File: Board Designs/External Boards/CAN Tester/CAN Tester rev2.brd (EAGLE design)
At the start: 83.8 x 100.3 mm, 27 parts, among them M1 Minifit, M2 Nanofit, M3 Nanofit-1, M4 Minifit-1, U1 ISOLATED CAN TRANSCIEVER, U3 TEENSY_3.2_SIMPLE, U4 CHARACTER_LCD

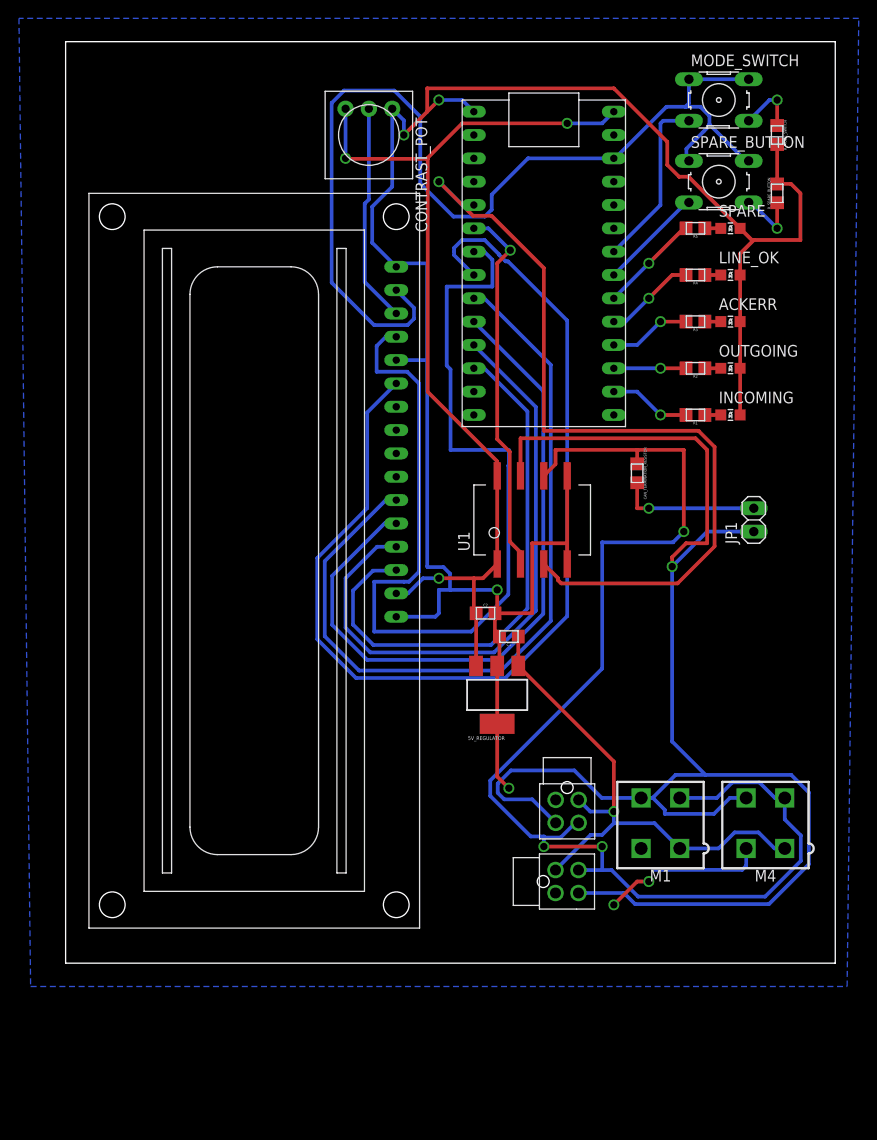
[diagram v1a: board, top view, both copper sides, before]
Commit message: Updated with true isolation for separate 5V for the isocan and teensy
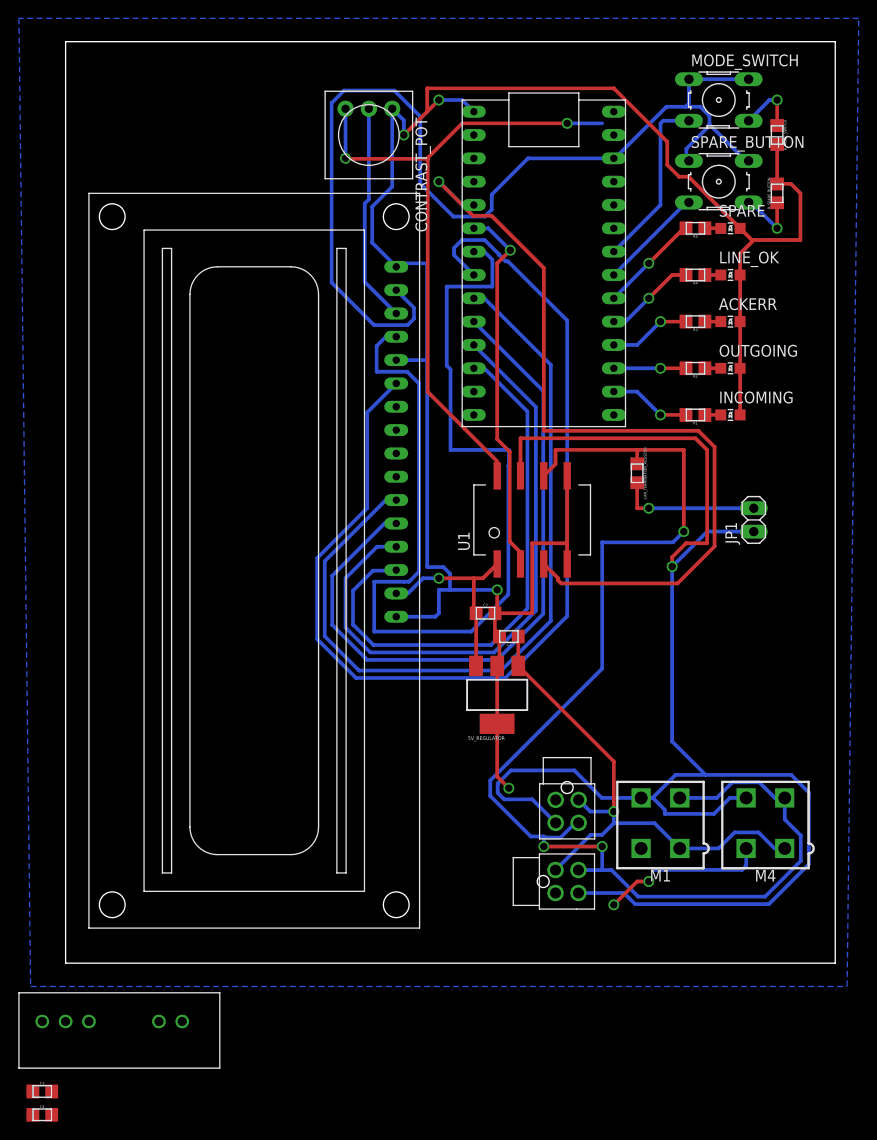
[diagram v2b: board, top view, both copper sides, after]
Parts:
- added C3, C4: 10 uF, HyTechDevices:0805
- added U$1: NCS1S1205SC-12V-5VCONVERTER, HyTechDevices:DCDC-CONVERTER
- R_MODE_SWITCH, R_SPARE_BUTTON: value 27K -> 10K
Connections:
- new net +5V_ISOLATED: C3.1, CONTRAST_POT.3, U$1.+VOUT, U1.P$1, U3.VIN, U4.15
- new net GND_ISOLATED: C3.2, U$1.-VOUT
- net +12V: now also C4.1, U$1.+VIN
- net +5V: no longer CONTRAST_POT.3, U1.P$1, U3.VIN, U4.15
- net GND: now also C4.2, U$1.-VIN
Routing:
- net +5V: track 106.1 -> 5.74 mm, vias 3 -> 0
- net +5V_ISOLATED: track 0.00 -> 87.0 mm, vias 0 -> 3
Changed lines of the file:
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@@
 <attribute name="VALUE" x="68.58" y="79.4512" size="0.3048" layer="27" rot="R180" align="top-center"/>
 </element>
-<element name="R_MODE_SWITCH" library="HyTechDevices" package="0805" value="27K" x="77.47" y="88.9" smashed="yes" rot="R270">
+<element name="R_MODE_SWITCH" library="HyTechDevices" package="0805" value="10K" x="77.47" y="88.9" smashed="yes" rot="R270">
 <attribute name="NAME" x="78.1939" y="88.9" size="0.3048" layer="25" rot="R270" align="bottom-center"/>
 <attribute name="VALUE" x="76.7588" y="88.9" size="0.3048" layer="27" rot="R270" align="top-center"/>
 </element>
-<element name="R_SPARE_BUTTON" library="HyTechDevices" package="0805" value="27K" x="77.47" y="82.55" smashed="yes" rot="R90">
+<element name="R_SPARE_BUTTON" library="HyTechDevices" package="0805" value="10K" x="77.47" y="82.55" smashed="yes" rot="R90">
 <attribute name="NAME" x="76.7461" y="82.55" size="0.3048" layer="25" rot="R90" align="bottom-center"/>
 <attribute name="VALUE" x="78.1812" y="82.55" size="0.3048" layer="27" rot="R90" align="top-center"/>
@@
 <attribute name="NAME" x="73.1012" y="44.3738" size="1.27" layer="25" ratio="10" rot="R90"/>
 <attribute name="VALUE" x="78.105" y="44.45" size="1.27" layer="27" rot="R90"/>
+</element>
+<element name="U$1" library="HyTechDevices" package="DCDC-CONVERTER" value="NCS1S1205SC-12V-5VCONVERTER" x="6.35" y="-7.62" smashed="yes"/>
+<element name="C3" library="HyTechDevices" package="0805" value="10 uF" x="-2.54" y="-15.24" smashed="yes">
+<attribute name="NAME" x="-2.54" y="-14.5161" size="0.3048" layer="25" align="bottom-center"/>
+<attribute name="VALUE" x="-2.54" y="-15.9512" size="0.3048" layer="27" align="top-center"/>
+</element>
+<element name="C4" library="HyTechDevices" package="0805" value="10 uF" x="-2.54" y="-17.78" smashed="yes">
+<attribute name="NAME" x="-2.54" y="-17.0561" size="0.3048" layer="25" align="bottom-center"/>
+<attribute name="VALUE" x="-2.54" y="-18.4912" size="0.3048" layer="27" align="top-center"/>
 </element>
 </elements>
@@
 <wire x1="50.8" y1="36.83" x2="50.8" y2="44.45" width="0.4064" layer="1"/>
 <wire x1="50.8" y1="44.45" x2="54.61" y2="44.45" width="0.4064" layer="1"/>
+<contactref element="C4" pad="2"/>
+<contactref element="U$1" pad="-VIN"/>
+<wire x1="63.94" y1="8.89" x2="62.67" y2="11.22" width="0" layer="19" extent="16-16"/>
+<wire x1="63.5" y1="7.62" x2="63.94" y2="8.89" width="0" layer="19" extent="16-16"/>
+<wire x1="53.34" y1="6.37" x2="59.69" y2="5.08" width="0" layer="19" extent="1-1"/>
+<wire x1="53.36" y1="16.51" x2="53.34" y2="6.37" width="0" layer="19" extent="1-1"/>
+<wire x1="48.26" y1="17.78" x2="53.36" y2="16.51" width="0" layer="19" extent="1-1"/>
+<wire x1="-2.54" y1="-7.62" x2="46.99" y2="19.05" width="0" layer="19" extent="1-1"/>
+<wire x1="-1.515" y1="-17.78" x2="-2.54" y2="-7.62" width="0" layer="19" extent="1-1"/>
 </signal>
 <signal name="CANH">
@@
 <wire x1="70.0024" y1="89.9414" x2="70.104" y2="90.043" width="0.4064" layer="16"/>
 </signal>
-<signal name="+5V">
-<contactref element="U3" pad="VIN"/>
-<contactref element="5V_REGULATOR" pad="3"/>
-<contactref element="C2" pad="1"/>
-<contactref element="U1" pad="P$1"/>
-<contactref element="U1" pad="P$8"/>
-<contactref element="U4" pad="15"/>
-<contactref element="CONTRAST_POT" pad="3"/>
-<wire x1="46.99" y1="42.19" x2="46.99" y2="51.79" width="0.4064" layer="1"/>
-<wire x1="46.99" y1="42.19" x2="45.44" y2="40.64" width="0.4064" layer="1"/>
-<wire x1="45.44" y1="40.64" x2="44.45" y2="40.64" width="0.4064" layer="1"/>
-<wire x1="44.45" y1="40.64" x2="44.45" y2="37.075" width="0.4064" layer="1"/>
-<wire x1="44.45" y1="37.075" x2="44.695" y2="36.83" width="0.4064" layer="1"/>
-<wire x1="44.695" y1="36.83" x2="44.695" y2="31.095" width="0.4064" layer="1"/>
-<wire x1="44.695" y1="31.095" x2="44.69" y2="31.09" width="0.4064" layer="1"/>
-<wire x1="44.45" y1="40.64" x2="40.64" y2="40.64" width="0.4064" layer="1"/>
-<via x="40.64" y="40.64" extent="1-16" drill="0.8" diameter="0.8"/>
-<wire x1="40.64" y1="40.64" x2="38.92" y2="40.64" width="0.4064" layer="16"/>
-<wire x1="38.92" y1="40.64" x2="37.27" y2="38.99" width="0.4064" layer="16"/>
-<wire x1="37.27" y1="38.99" x2="36" y2="38.99" width="0.4064" layer="16"/>
-<wire x1="46.99" y1="51.79" x2="46.99" y2="53.36670625" width="0.4064" layer="1"/>
-<wire x1="39.4272" y1="86.3028" x2="39.37" y2="86.36" width="0.4064" layer="1"/>
-<wire x1="46.99" y1="53.36670625" x2="39.4272" y2="60.92950625" width="0.4064" layer="1"/>
-<wire x1="39.4272" y1="60.92950625" x2="39.4272" y2="86.3028" width="0.4064" layer="1"/>
-<wire x1="39.37" y1="86.36" x2="43.18" y2="90.17" width="0.4064" layer="1"/>
-<wire x1="43.18" y1="90.17" x2="54.61" y2="90.17" width="0.4064" layer="1"/>
-<via x="54.61" y="90.17" extent="1-16" drill="0.8" diameter="0.8"/>
-<wire x1="54.61" y1="90.17" x2="58.42" y2="90.17" width="0.4064" layer="16"/>
-<wire x1="58.42" y1="90.17" x2="59.69" y2="91.44" width="0.4064" layer="16"/>
-<wire x1="39.4272" y1="86.3028" x2="30.5372" y2="86.3028" width="0.4064" layer="1"/>
-<wire x1="30.5372" y1="86.3028" x2="30.48" y2="86.36" width="0.4064" layer="1"/>
-<via x="30.48" y="86.36" extent="1-16" drill="0.8" diameter="0.8"/>
-<wire x1="30.48" y1="86.36" x2="30.48" y2="91.7575" width="0.4064" layer="16"/>
-</signal>
 <signal name="N$13">
 <contactref element="U3" pad="A6"/>
@@
 <wire x1="58.42" y1="12.7" x2="59.69" y2="13.97" width="0.4064" layer="16"/>
 <wire x1="57.17" y1="12.7" x2="58.42" y2="12.7" width="0.4064" layer="16"/>
+<contactref element="C4" pad="1"/>
+<contactref element="U$1" pad="+VIN"/>
+<wire x1="0" y1="-7.62" x2="53.34" y2="8.87" width="0" layer="19" extent="1-1"/>
+<wire x1="-3.565" y1="-17.78" x2="0" y2="-7.62" width="0" layer="19" extent="1-1"/>
 </signal>
 <signal name="N$12">
@@
 <wire x1="63.5" y1="48.26" x2="74.93" y2="48.26" width="0.4064" layer="16"/>
 </signal>
+<signal name="+5V_ISOLATED">
+<contactref element="U$1" pad="+VOUT"/>
+<contactref element="C3" pad="1"/>
+<contactref element="U3" pad="VIN"/>
+<contactref element="U1" pad="P$1"/>
+<contactref element="U4" pad="15"/>
+<contactref element="CONTRAST_POT" pad="3"/>
+<wire x1="46.99" y1="42.19" x2="45.44" y2="40.64" width="0.4064" layer="1"/>
+<wire x1="45.44" y1="40.64" x2="44.45" y2="40.64" width="0.4064" layer="1"/>
+<wire x1="44.45" y1="40.64" x2="44.45" y2="37.075" width="0.4064" layer="1"/>
+<wire x1="44.45" y1="40.64" x2="40.64" y2="40.64" width="0.4064" layer="1"/>
+<via x="40.64" y="40.64" extent="1-16" drill="0.8" diameter="0.8"/>
+<wire x1="40.64" y1="40.64" x2="38.92" y2="40.64" width="0.4064" layer="16"/>
+<wire x1="38.92" y1="40.64" x2="37.27" y2="38.99" width="0.4064" layer="16"/>
+<wire x1="37.27" y1="38.99" x2="36" y2="38.99" width="0.4064" layer="16"/>
+<wire x1="39.4272" y1="86.3028" x2="39.37" y2="86.36" width="0.4064" layer="1"/>
+<wire x1="46.99" y1="53.36670625" x2="39.4272" y2="60.92950625" width="0.4064" layer="1"/>
+<wire x1="39.4272" y1="60.92950625" x2="39.4272" y2="86.3028" width="0.4064" layer="1"/>
+<wire x1="39.37" y1="86.36" x2="43.18" y2="90.17" width="0.4064" layer="1"/>
+<wire x1="43.18" y1="90.17" x2="54.61" y2="90.17" width="0.4064" layer="1"/>
+<via x="54.61" y="90.17" extent="1-16" drill="0.8" diameter="0.8"/>
+<wire x1="54.61" y1="90.17" x2="58.42" y2="90.17" width="0.4064" layer="16"/>
+<wire x1="39.4272" y1="86.3028" x2="30.5372" y2="86.3028" width="0.4064" layer="1"/>
+<wire x1="30.5372" y1="86.3028" x2="30.48" y2="86.36" width="0.4064" layer="1"/>
+<via x="30.48" y="86.36" extent="1-16" drill="0.8" diameter="0.8"/>
+<wire x1="30.48" y1="86.36" x2="30.48" y2="91.7575" width="0.4064" layer="16"/>
+<wire x1="58.42" y1="90.17" x2="59.69" y2="91.44" width="0" layer="19" extent="16-16"/>
+<wire x1="46.99" y1="42.19" x2="46.99" y2="53.36670625" width="0" layer="19" extent="1-1"/>
+<wire x1="10.16" y1="-7.62" x2="36" y2="38.99" width="0" layer="19" extent="1-1"/>
+<wire x1="-3.565" y1="-15.24" x2="10.16" y2="-7.62" width="0" layer="19" extent="1-1"/>
+</signal>
+<signal name="GND_ISOLATED">
+<contactref element="C3" pad="2"/>
+<contactref element="U$1" pad="-VOUT"/>
+<wire x1="12.7" y1="-7.62" x2="-1.515" y2="-15.24" width="0" layer="19" extent="1-1"/>
+</signal>
+<signal name="+5V">
+<contactref element="5V_REGULATOR" pad="3"/>
+<contactref element="C2" pad="1"/>
+<wire x1="44.695" y1="36.83" x2="44.695" y2="31.095" width="0.4064" layer="1"/>
+<wire x1="44.695" y1="31.095" x2="44.69" y2="31.09" width="0.4064" layer="1"/>
+<contactref element="U1" pad="P$8"/>
+<wire x1="44.695" y1="36.83" x2="46.99" y2="51.79" width="0" layer="19" extent="1-1"/>
+</signal>
 </signals>

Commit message: Finished isolating and started work on fixing CAN_Tester board
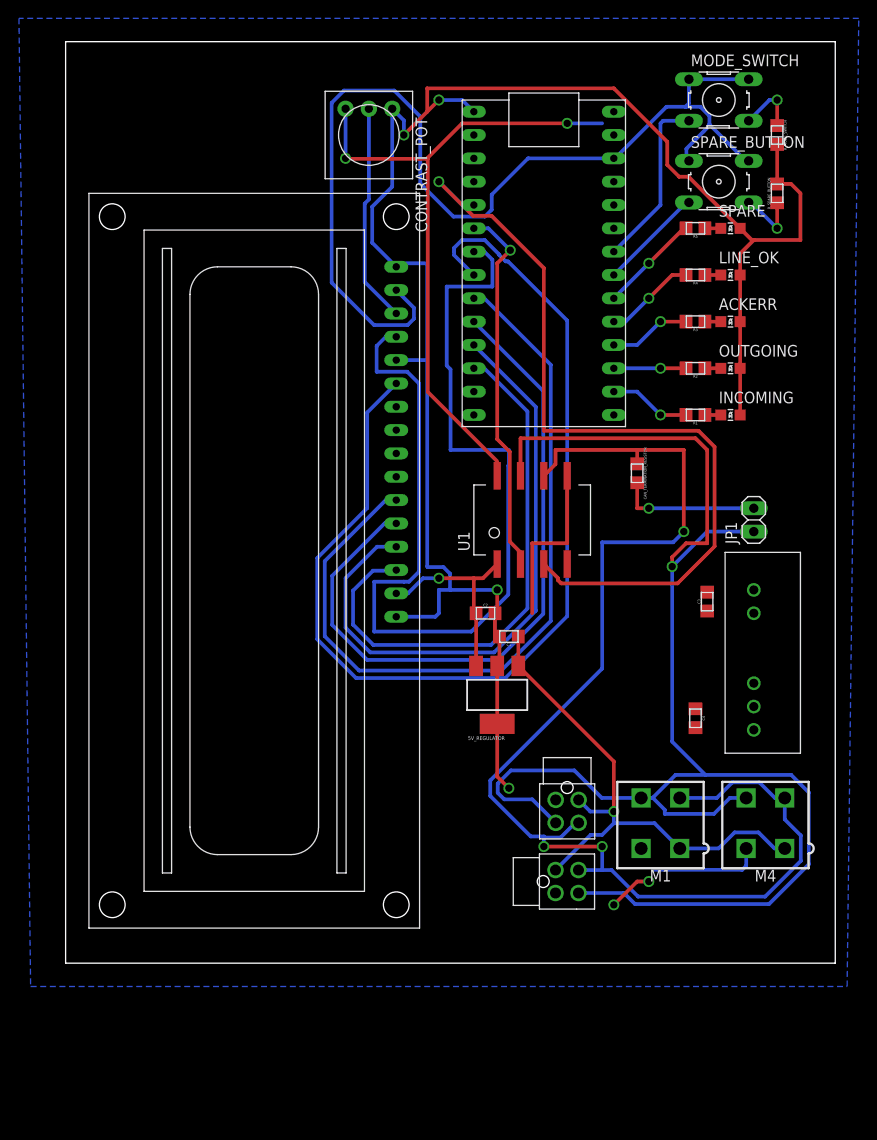
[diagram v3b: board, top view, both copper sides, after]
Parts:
- moved C3 89.9 mm to (69.8, 38.1), turned to 90 degrees
- moved C4 83.2 mm to (68.6, 25.4), turned to 270 degrees
- moved U$1 79.7 mm to (74.9, 33.0), turned to 90 degrees
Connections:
- net GND: no longer ACKERR.C, CONTRAST_POT.1, INCOMING.C, LINE_OK.C, OUTGOING.C, R_MODE_SWITCH.2, R_SPARE_BUTTON.2, SPARE.C, U1.P$4, U3.GND, U4.1, U4.16, U4.5
- net GND_ISOLATED: now also ACKERR.C, CONTRAST_POT.1, INCOMING.C, LINE_OK.C, OUTGOING.C, R_MODE_SWITCH.2, R_SPARE_BUTTON.2, SPARE.C, U1.P$4, U3.GND, U4.1, U4.16, U4.5
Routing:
- net GND: track 238.7 -> 50.9 mm, vias 6 -> 1
- net GND_ISOLATED: track 0.00 -> 181.2 mm, vias 0 -> 5
- added copper zone on layer 16, net GND_ISOLATED
- removed copper zone on layer 16, net GND

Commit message: Fixed circuit to have true isolation in CAN_Tester, and started work on new board layout
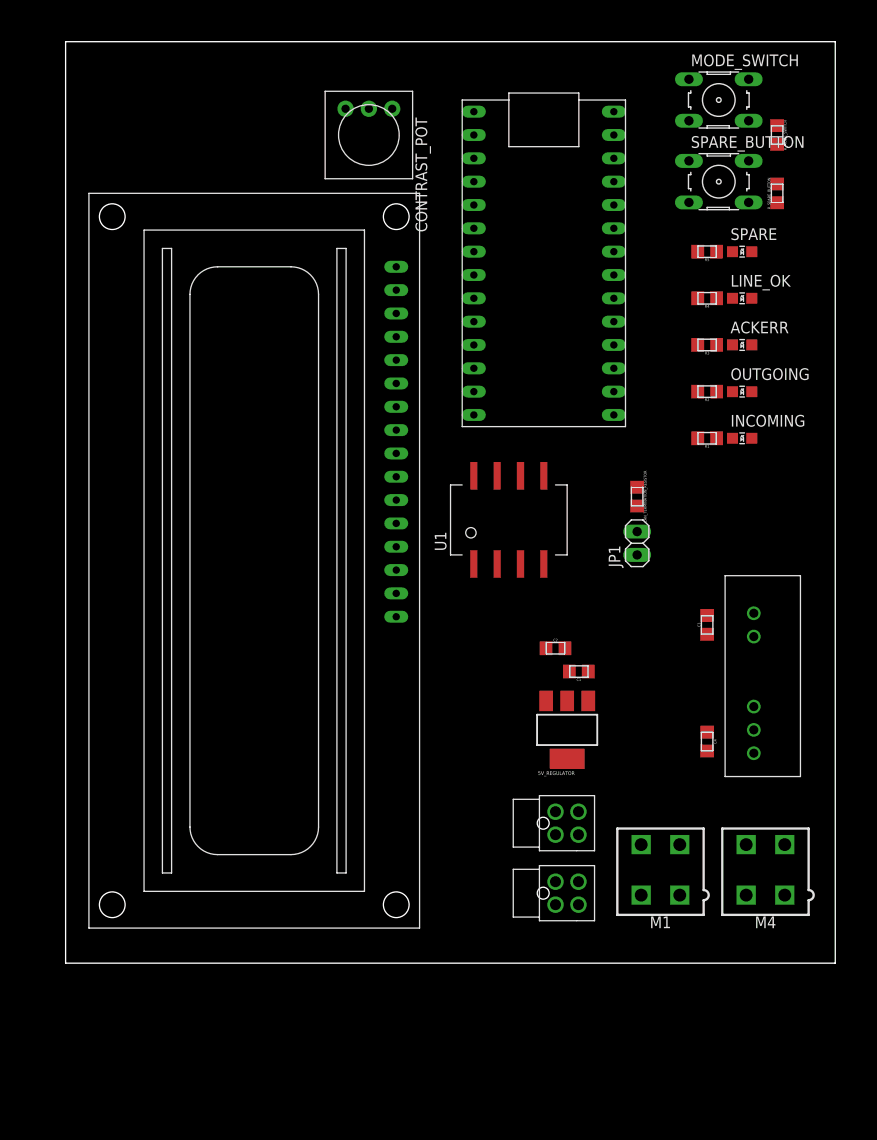
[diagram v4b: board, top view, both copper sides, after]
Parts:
- M1: value Minifit -> Minifit-1
- M2: value Nanofit -> Nanofit-1
- M3: value Nanofit-1 -> Nanofit-2
- M4: value Minifit-1 -> Minifit-2
- moved JP1 13.0 mm to (62.2, 44.5)
- moved C1 8.52 mm to (55.9, 30.5)
- moved C2 8.52 mm to (53.3, 33.0)
- moved 5V_REGULATOR 8.52 mm to (54.6, 24.1)
- moved M1 5.08 mm to (64.8, 8.89)
- moved M4 5.08 mm to (76.2, 8.89)
- moved M3 2.84 mm to (53.3, 14.0), turned to 270 degrees
- moved C4 2.84 mm to (69.8, 22.9)
- moved INCOMING 2.84 mm to (73.7, 55.9)
- moved OUTGOING 2.84 mm to (73.7, 61.0)
- moved R1 2.84 mm to (69.8, 55.9)
- moved R2 2.84 mm to (69.8, 61.0)
- moved ACKERR 2.84 mm to (73.7, 66.0)
- moved LINE_OK 2.84 mm to (73.7, 71.1)
- moved R3 2.84 mm to (69.8, 66.0)
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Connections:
- net +3V3: now also CONTRAST_POT.3, U4.15
- net +5V_ISOLATED: no longer CONTRAST_POT.3, U4.15
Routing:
- net GND_ISOLATED: track 181.2 -> 0.00 mm, vias 5 -> 0
- net CANH: track 168.5 -> 0.00 mm, vias 1 -> 0
- net CANL: track 139.3 -> 0.00 mm, vias 3 -> 0
- net N$18: track 115.5 -> 0.00 mm
- net +3V3: track 114.2 -> 0.00 mm
- net N$17: track 108.4 -> 0.00 mm
- net CANTX: track 89.3 -> 0.00 mm, vias 1 -> 0
- net +5V_ISOLATED: track 87.0 -> 0.00 mm, vias 3 -> 0
- net N$19: track 86.4 -> 0.00 mm
- net N$20: track 76.3 -> 0.00 mm
- net N$21: track 67.8 -> 0.00 mm
- net N$22: track 60.1 -> 0.00 mm
- net +12V: track 58.6 -> 0.00 mm, vias 1 -> 0
- net GND: track 50.9 -> 0.00 mm, vias 1 -> 0
- net CANRX: track 40.8 -> 0.00 mm, vias 1 -> 0
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- removed copper zone on layer 16, net GND_ISOLATED
